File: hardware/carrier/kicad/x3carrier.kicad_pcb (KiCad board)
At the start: 2 copper layers, 38 x 50 mm, 37 parts, among them J1 Sockel SuperMini, J2 Sockel SuperMini, J3 AKKU, J4 SWD-ZIEL, Q1 AO3401A, Q2 AO3401A, SW1 EIN/AUS, U1 TP4056

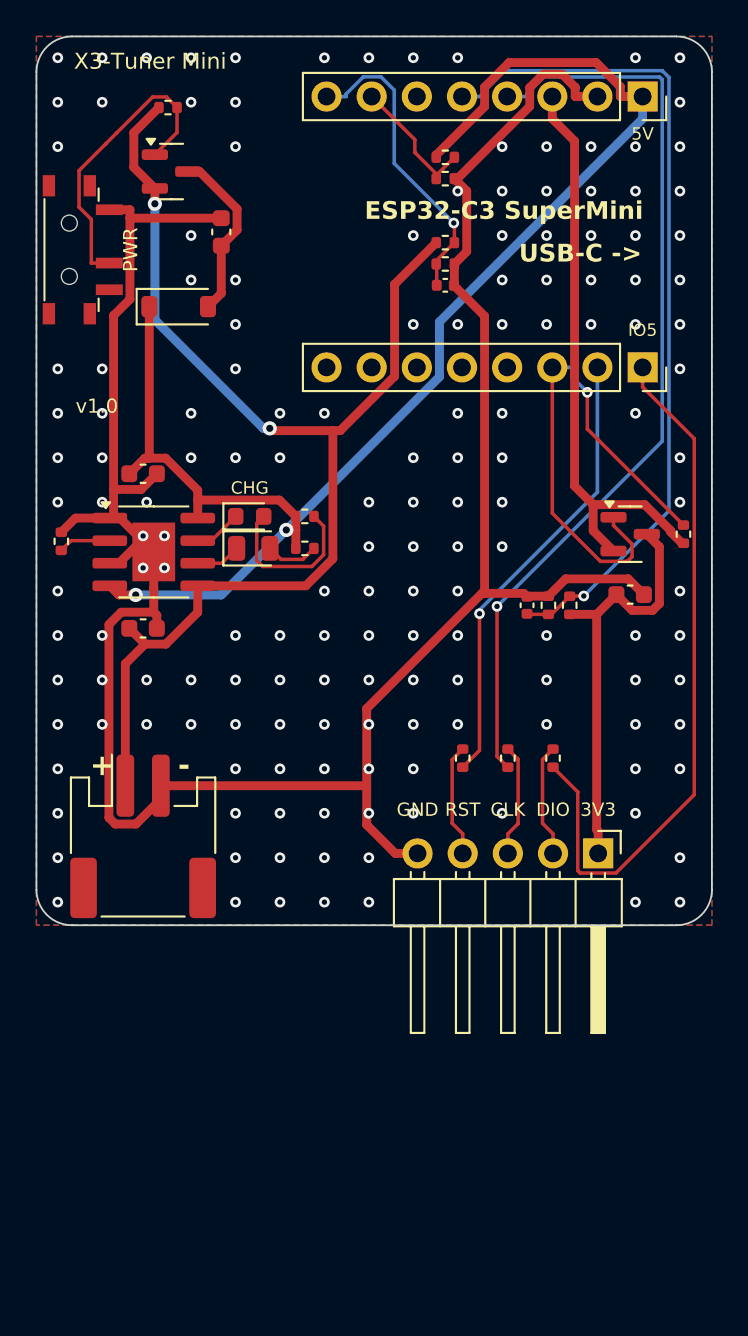
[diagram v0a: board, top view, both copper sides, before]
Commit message: X3-Tuner Mini as a stick: narrow carrier board and 3D-printed case
Carrier board (Rev 1.1) redesigned as a 20.5 x 65 mm stick: the
SuperMini sits at the front with its USB-C in the end face, the SWD
header at the rear, the charger between the socket rows. New P-MOSFET
Q3 as battery reverse-polarity protection (cheap JST-PH cells often
have swapped leads), charge current lowered to ~235 mA (R1 = 5.1k) for
300-400 mAh cells. Routed, DRC clean; panel and NextPCB rail variant
(12 mm rails, 50.6 x 65 mm) regenerated.

Case: the X3-Tuner case model is now a shared core (case_core.scad)
with one small wrapper per board; the X3-Tuner STLs are unchanged.
New options for the stick: USB-C in the end face, battery pocket under
the lid, ribs pressing the SuperMini into its sockets, windows over its
LEDs/buttons, pin labels above the SWD slot. make_case_data.py and
make_case.sh build either board via X3_CIRCUIT. The Mini case is
77.7 x 24.4 x 22.4 mm for an 802030 LiPo and was checked for collisions
with board, SuperMini and battery.

Co-Authored-By: Claude Opus 5.5 <noreply@anthropic.com>
Claude-Session: https://claude.ai/code/session_01RVwXhv4cRLa5H5kfiVg79q
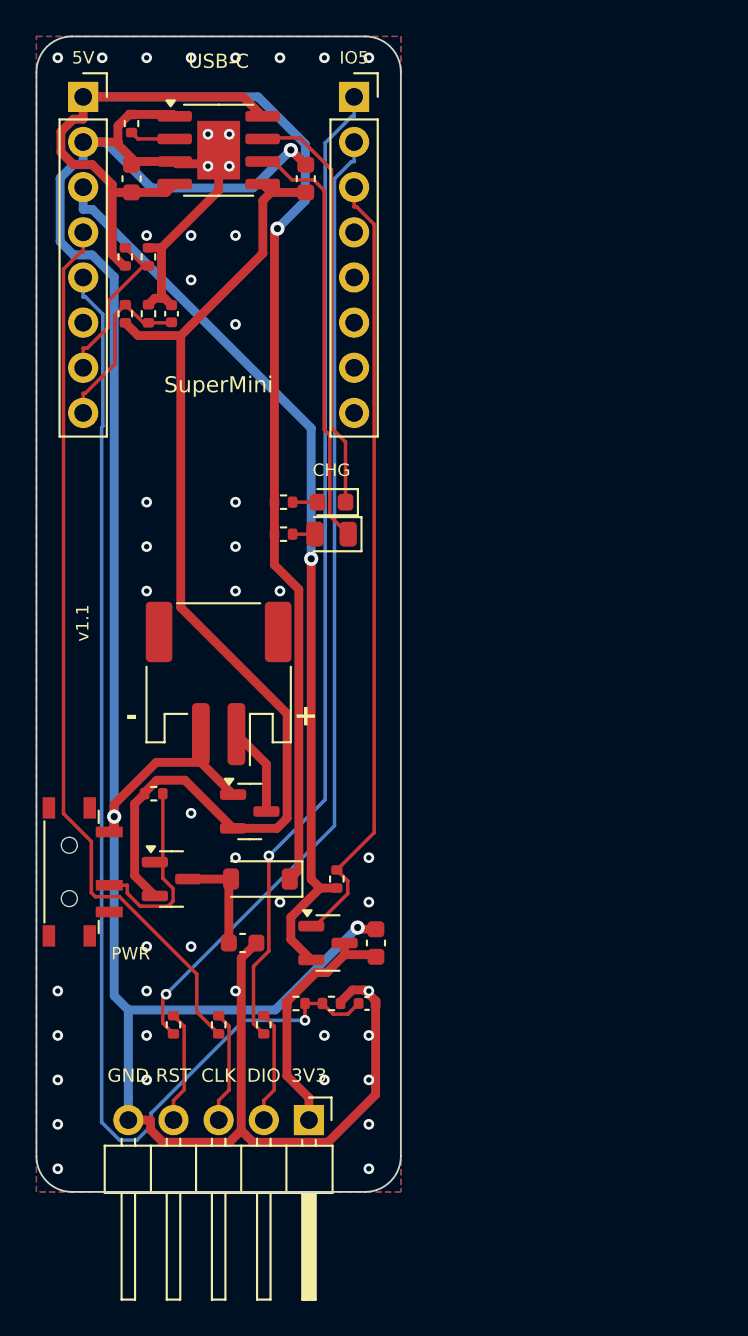
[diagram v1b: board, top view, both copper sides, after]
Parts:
- added KT7: Tab, kikit:Tab, F.Cu at (110.2, 61.5)
- added Q3: AO3401A, Package_TO_SOT_SMD:SOT-23, F.Cu at (112.0, 103.6)
- R1: value 3.3k -> 5.1k
- moved KT3 48.8 mm to (101.5, 118.0), turned to 180 degrees
- moved C3 40.0 mm to (111.6, 111.0), turned to 0 degrees
- moved Q1 39.8 mm to (107.6, 107.4)
- moved R4 38.6 mm to (106.6, 102.6)
- moved SW1 35.0 mm to (102.4, 107.0)
- moved KT5 34.1 mm to (119.0, 93.0), turned to 0 degrees
- moved D1 32.5 mm to (112.6, 107.4), turned to 180 degrees
- moved J1 31.5 mm to (102.6, 63.4), turned to 0 degrees
- moved KT4 31.3 mm to (119.0, 72.0)
- moved Q2 28.6 mm to (116.4, 111.0)
- moved R5 27.5 mm to (116.9, 107.4)
- moved R6 27.2 mm to (114.6, 114.4), turned to 0 degrees
- moved C2 26.9 mm to (115.2, 68.0), turned to 90 degrees
- moved R7 25.5 mm to (116.6, 114.4), turned to 0 degrees
- moved C4 24.3 mm to (119.1, 111.0), turned to 90 degrees
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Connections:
- J3 pad 1: VBAT -> BAT_IN
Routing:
- net NRST: track 25.6 -> 55.0 mm
- net GND: track 135.3 -> 160.5 mm, vias 160 -> 50
- net STDBY: track 2.53 -> 24.0 mm
- net CHRG: track 2.70 -> 23.7 mm
- net VTGT_SENSE: track 47.3 -> 67.6 mm
- net +3V3: track 33.0 -> 51.4 mm, vias 0 -> 1
- net SWDIO: track 40.1 -> 55.4 mm, vias 0 -> 1
- net TGT_EN: track 29.1 -> 44.2 mm, vias 1 -> 0
- net VTGT: track 23.7 -> 14.0 mm
- net LED_R_A: track 9.20 -> 1.40 mm
- net VBAT_SENSE: track 17.5 -> 10.2 mm, vias 1 -> 0
- net VBAT: track 69.1 -> 62.0 mm, vias 2 -> 0
- net PWR_G: track 17.1 -> 11.2 mm
- net BAT_IN: track 0.00 -> 5.05 mm
- net VBAT_SW: track 9.79 -> 6.01 mm
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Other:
- board size 38 x 50 mm -> 20.5 x 65 mm
- board text added: "Akku: 1S LiPo MIT Schutz, + = Pin 1"
- board text added: "SuperMini"
- board text added: "SuperMini: USB-C zur Stirnseite"
- board text added: "USB-C"
- board text added: "X3-Tuner Mini v1.1"
- board text added: "v1.1"
- board text removed: "Akku: 1S LiPo MIT Schutzschaltung, + = Pin 1"
- board text removed: "ESP32-C3 SuperMini"
- board text removed: "SuperMini: USB-C zur rechten Kante"
- board text removed: "USB-C ->"
- board text removed: "X3-Tuner Mini"
- board text removed: "X3-Tuner Mini v1.0"
- board text removed: "v1.0"

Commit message: X3-Tuner Mini Rev 1.2: pin headers, closed case, Wi-Fi OTA + flash lock
The ESP32-C3 SuperMini has no pins, so the carrier now carries two 1x8
male headers (factory-soldered); the module is pushed on and clamped by
the lid. Same pads/routing as the sockets, DRC clean; panel and NextPCB
variant regenerated. The header's LCSC number could not be verified
(jlcpcb.com unreachable) and is left blank in the BOM; make_fab/make_panel
now keep LCSC-less parts in the BOM/CPL and warn, instead of silently
dropping them.

Case: no openings over the SuperMini — RESET/BOOT are unreachable and the
module is fully enclosed. The module sits flat on the headers (not on tall
sockets), so the case is driven by the lid battery and drops to 20.9 mm.
Battery pocket now for a 6-7 mm cell (clears the JST socket); the clamp is
split into two ribs that avoid the chip antenna. Collision-checked against
board, SuperMini and battery.

Firmware: Wi-Fi OTA endpoint (src/ota.h, POST /api/ota) on the x3carrier
build with an OTA-capable partition, so the app can update the device with
USB download mode locked. hardware/carrier/SECURITY.md documents the
one-time eFuse hardening (flash encryption, Secure Boot v2, disabling the
download mode) that makes the firmware non-readable and non-flashable while
keeping signed OTA updates.

Co-Authored-By: Claude Opus 4.8 <noreply@anthropic.com>
Claude-Session: https://claude.ai/code/session_01RVwXhv4cRLa5H5kfiVg79q
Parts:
- J1, J2: value Sockel SuperMini -> Stift SuperMini; footprint Connector_PinSocket_2.54mm:PinSocket_1x08_P2.54mm_Vertical -> Connector_PinHeader_2.54mm:PinHeader_1x08_P2.54mm_Vertical
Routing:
- net SWCLK: track 50.0 -> 63.9 mm
- net GND: track 160.5 -> 171.6 mm, vias 50 -> 60
- net VBUS: track 83.2 -> 72.2 mm, vias 1 -> 2
- net VBAT: track 62.0 -> 54.1 mm, vias 0 -> 2
- net NRST: track 55.0 -> 59.8 mm
- net PWR_G: track 11.2 -> 7.14 mm
- net SWDIO: track 55.4 -> 57.7 mm, vias 1 -> 0
- net CHRG: track 23.7 -> 22.7 mm, vias 0 -> 2
- net +3V3: track 51.4 -> 50.5 mm, vias 1 -> 2
- net VTGT_SENSE: track 67.6 -> 68.3 mm, vias 1 -> 2
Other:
- board text added: "X3-Tuner Mini v1.2"
- board text added: "v1.2"
- board text removed: "X3-Tuner Mini v1.1"
- board text removed: "v1.1"
